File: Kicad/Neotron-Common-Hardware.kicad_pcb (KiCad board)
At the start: 4 copper layers, 243.8 x 243.8 mm, 210 parts, among them J1001 SD_Card, J101 Neotron-Expansion-Slot, J102 Neotron-Expansion-Slot, J103 Neotron-Expansion-Slot, J104 Neotron-Expansion-Slot, J201 DE15HD, J301 RJ45 MagJack, J401 CD Audio In, J402 AC'97 Audio Header, J403 Line Out, J501 USB Ports External, J502 USB Ports Internal, J601 Jack-DC, J602 Conn_01x04, J603 Double-mini-DIN-6, J801 Conn_02x05, J802 DB9_Male_MountingHoles, SW601 SW_DIP_x01, SW602 SW_DIP_x01, U101 Neotron-CPU, U201 THS7316, U202 TPD7S019, U301 ENC424J600, U401 TLV320AIC23BPW, U402 STX-4335-5BGP-S1, U501 AP2501, U502 MIC2005A-2YM5, U503 MIC2005A-2YM5, U504 XR22404CG28, U505 MIC2005A-2YM5, U506 MIC2005A-2YM5, U601 5V DC-DC Module, U602 3v3 LDO, U603 MAX1615, U604 MKE04P24M48SF0, U801 ST3232CDR, U901 MCP7940, Y301 25M, Y401 12M, Y501 12M, Y901 32,768 Hz

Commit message: Updated PCB with latest netlist.
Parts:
- added R301: 24k 0.5%, Resistor_SMD:R_0805_2012Metric_Pad1.15x1.40mm_HandSolder, F.Cu at (54.7, 116.4)
- added R302: 24k 0.5%, Resistor_SMD:R_0805_2012Metric_Pad1.15x1.40mm_HandSolder, F.Cu at (68.9, 116.4)
- added R303: 24k 0.5%, Resistor_SMD:R_0805_2012Metric_Pad1.15x1.40mm_HandSolder, F.Cu at (64.2, 119.3)
- added R304: 24k 0.5%, Resistor_SMD:R_0805_2012Metric_Pad1.15x1.40mm_HandSolder, F.Cu at (59.4, 122.3)
- added R305: 24k 0.5%, Resistor_SMD:R_0805_2012Metric_Pad1.15x1.40mm_HandSolder, F.Cu at (68.9, 113.4)
- added R306: 24k 0.5%, Resistor_SMD:R_0805_2012Metric_Pad1.15x1.40mm_HandSolder, F.Cu at (64.2, 116.4)
- added R307: 12k 0.5%, Resistor_SMD:R_0805_2012Metric_Pad1.15x1.40mm_HandSolder, F.Cu at (59.4, 119.3)
- added R308: 12k 0.5%, Resistor_SMD:R_0805_2012Metric_Pad1.15x1.40mm_HandSolder, F.Cu at (54.7, 122.3)
- added R309: 12k 0.5%, Resistor_SMD:R_0805_2012Metric_Pad1.15x1.40mm_HandSolder, F.Cu at (64.2, 113.4)
- added R310: 12k 0.5%, Resistor_SMD:R_0805_2012Metric_Pad1.15x1.40mm_HandSolder, F.Cu at (59.4, 116.4)
- added R311: 12k 0.5%, Resistor_SMD:R_0805_2012Metric_Pad1.15x1.40mm_HandSolder, F.Cu at (54.7, 113.4)
- added R312: 24k 0.5%, Resistor_SMD:R_0805_2012Metric_Pad1.15x1.40mm_HandSolder, F.Cu at (54.7, 119.3)
- added R313: 3300, Resistor_SMD:R_0805_2012Metric_Pad1.15x1.40mm_HandSolder, F.Cu at (59.4, 113.4)
- added R401: 24k 0.5%, Resistor_SMD:R_0805_2012Metric_Pad1.15x1.40mm_HandSolder, F.Cu at (64.2, 134.6)
- added R402: 24k 0.5%, Resistor_SMD:R_0805_2012Metric_Pad1.15x1.40mm_HandSolder, F.Cu at (59.4, 137.5)
- added R403: 24k 0.5%, Resistor_SMD:R_0805_2012Metric_Pad1.15x1.40mm_HandSolder, F.Cu at (68.9, 128.7)
- added R404: 24k 0.5%, Resistor_SMD:R_0805_2012Metric_Pad1.15x1.40mm_HandSolder, F.Cu at (64.2, 131.6)
- added R405: 24k 0.5%, Resistor_SMD:R_0805_2012Metric_Pad1.15x1.40mm_HandSolder, F.Cu at (59.4, 134.6)
- added R406: 24k 0.5%, Resistor_SMD:R_0805_2012Metric_Pad1.15x1.40mm_HandSolder, F.Cu at (68.9, 131.6)
- added R407: 12k 0.5%, Resistor_SMD:R_0805_2012Metric_Pad1.15x1.40mm_HandSolder, F.Cu at (54.7, 128.7)
- added R408: 12k 0.5%, Resistor_SMD:R_0805_2012Metric_Pad1.15x1.40mm_HandSolder, F.Cu at (54.7, 137.5)
- added R409: 12k 0.5%, Resistor_SMD:R_0805_2012Metric_Pad1.15x1.40mm_HandSolder, F.Cu at (64.2, 128.7)
- added R410: 12k 0.5%, Resistor_SMD:R_0805_2012Metric_Pad1.15x1.40mm_HandSolder, F.Cu at (59.4, 131.6)
- added R411: 12k 0.5%, Resistor_SMD:R_0805_2012Metric_Pad1.15x1.40mm_HandSolder, F.Cu at (54.7, 134.6)
- added R412: 24k 0.5%, Resistor_SMD:R_0805_2012Metric_Pad1.15x1.40mm_HandSolder, F.Cu at (59.4, 128.7)
- added R413: 3300, Resistor_SMD:R_0805_2012Metric_Pad1.15x1.40mm_HandSolder, F.Cu at (54.7, 131.6)
- added R501: 24k 0.5%, Resistor_SMD:R_0805_2012Metric_Pad1.15x1.40mm_HandSolder, F.Cu at (93.7, 116.4)
- added R502: 24k 0.5%, Resistor_SMD:R_0805_2012Metric_Pad1.15x1.40mm_HandSolder, F.Cu at (89.0, 119.3)
- added R503: 24k 0.5%, Resistor_SMD:R_0805_2012Metric_Pad1.15x1.40mm_HandSolder, F.Cu at (84.2, 122.3)
- added R504: 24k 0.5%, Resistor_SMD:R_0805_2012Metric_Pad1.15x1.40mm_HandSolder, F.Cu at (93.7, 113.4)
- added R505: 24k 0.5%, Resistor_SMD:R_0805_2012Metric_Pad1.15x1.40mm_HandSolder, F.Cu at (89.0, 116.4)
- added R506: 24k 0.5%, Resistor_SMD:R_0805_2012Metric_Pad1.15x1.40mm_HandSolder, F.Cu at (84.2, 119.3)
- added R507: 12k 0.5%, Resistor_SMD:R_0805_2012Metric_Pad1.15x1.40mm_HandSolder, F.Cu at (79.5, 122.3)
- added R508: 12k 0.5%, Resistor_SMD:R_0805_2012Metric_Pad1.15x1.40mm_HandSolder, F.Cu at (89.0, 113.4)
- added R509: 12k 0.5%, Resistor_SMD:R_0805_2012Metric_Pad1.15x1.40mm_HandSolder, F.Cu at (84.2, 116.4)
- added R510: 12k 0.5%, Resistor_SMD:R_0805_2012Metric_Pad1.15x1.40mm_HandSolder, F.Cu at (79.5, 119.3)
- added R511: 12k 0.5%, Resistor_SMD:R_0805_2012Metric_Pad1.15x1.40mm_HandSolder, F.Cu at (84.2, 113.4)
- added R512: 24k 0.5%, Resistor_SMD:R_0805_2012Metric_Pad1.15x1.40mm_HandSolder, F.Cu at (79.5, 116.4)
- added R513: 3300, Resistor_SMD:R_0805_2012Metric_Pad1.15x1.40mm_HandSolder, F.Cu at (79.5, 113.4)
- C1006: renamed from C504; footprint Capacitor_THT:CP_Radial_D6.3mm_P2.50mm -> Capacitor_THT:CP_Radial_D8.0mm_P3.50mm
- C1007: renamed from C505; footprint Capacitor_THT:CP_Radial_D6.3mm_P2.50mm -> Capacitor_THT:CP_Radial_D8.0mm_P3.50mm
- C1010: renamed from C509; footprint Capacitor_THT:CP_Radial_D6.3mm_P2.50mm -> Capacitor_THT:CP_Radial_D8.0mm_P3.50mm
- C1011: renamed from C510; footprint Capacitor_THT:CP_Radial_D6.3mm_P2.50mm -> Capacitor_THT:CP_Radial_D8.0mm_P3.50mm
- C901: renamed from C601; footprint Capacitor_THT:CP_Radial_D6.3mm_P2.50mm -> Capacitor_THT:CP_Radial_D8.0mm_P3.50mm
- C902: renamed from C602; footprint Capacitor_THT:CP_Radial_D6.3mm_P2.50mm -> Capacitor_THT:CP_Radial_D8.0mm_P3.50mm
- J802: footprint Connector_Dsub:DSUB-9_Male_Horizontal_P2.77x2.84mm_EdgePinOffset4.94mm_Housed_MountingHolesOffset7.48mm -> Connector_Dsub:DSUB-9_Male_Horizontal_P2.77x2.84mm_EdgePinOffset7.70mm_Housed_MountingHolesOffset9.12mm
- renumbered BT901 to BT1201, C501 to C1001, C508 to C1002, C511 to C1003, C502 to C1004, C503 to C1005, C506 to C1008, C507 to C1009, C310 to C1101, C311 to C1102, C309 to C1103, C312 to C1104, C308 to C1105, C301 to C1106, C302 to C1107, C303 to C1108, C304 to C1109, C305 to C1110, C306 to C1111, C307 to C1112, C901 to C1201, C902 to C1202, C903 to C1203, C412 to C601, C413 to C602, C407 to C603, C411 to C604, C418 to C605, C419 to C606, C424 to C607, C427 to C608, C431 to C609, C435 to C610, C402 to C611, C406 to C612, C408 to C613, C420 to C614, C421 to C615, C426 to C616, C428 to C617, C432 to C618, C437 to C619, C422 to C620, C423 to C621, C430 to C622, C433 to C623, C436 to C624, C438 to C625, C415 to C626, C416 to C627, C401 to C628, C405 to C629, C425 to C630, C429 to C631, C434 to C632, C403 to C633, C409 to C634, C414 to C635, C417 to C636, C404 to C637, C410 to C638, C1001 to C701, C1002 to C702, C802 to C801, C803 to C802, C805 to C803, C801 to C805, C603 to C903, C604 to C904, C605 to C905, C606 to C906, C607 to C907, C608 to C908, D601 to D901, F601 to F901, FB405 to FB601, FB409 to FB602, FB406 to FB603, FB410 to FB604, FB408 to FB605, FB411 to FB606, FB407 to FB607, FB401 to FB608, FB403 to FB609, FB402 to FB610, FB404 to FB611, J501 to J1001, J502 to J1002, J301 to J1101, J403 to J601, J402 to J602, J401 to J603, J1001 to J701, J601 to J901, J602 to J902, J603 to J903, L601 to L901, LOGO103 to LOGO101, LOGO101 to LOGO103, R502 to R1001, R501 to R1002, R503 to R1003, R504 to R1004, R507 to R1005, R508 to R1006, R509 to R1007, R506 to R1008, R302 to R1101, R308 to R1102, R303 to R1103, R304 to R1104, R301 to R1105, R309 to R1106, R305 to R1107, R311 to R1108, R310 to R1109, R312 to R1110, R307 to R1111, R306 to R1112, R209 to R207, R207 to R208, R208 to R209, R404 to R601, R405 to R602, R406 to R603, R409 to R604, R407 to R605, R410 to R606, R414 to R607, R415 to R608, R408 to R609, R413 to R610, R411 to R611, R412 to R612, R416 to R613, R401 to R614, R403 to R615, R402 to R616, R601 to R901, R602 to R902, R603 to R903, R604 to R904, R606 to R905, R605 to R906, R608 to R907, R607 to R908, RN1001 to RN701, RN601 to RN901, SW601 to SW901, SW602 to SW902, TP601 to TP901, U501 to U1001, U502 to U1002, U503 to U1003, U504 to U1004, U505 to U1005, U506 to U1006, U301 to U1101, U901 to U1201, U401 to U601, U402 to U602, U601 to U901, U602 to U902, U603 to U903, U604 to U904, Y501 to Y1001, Y301 to Y1101, Y901 to Y1201, Y401 to Y601

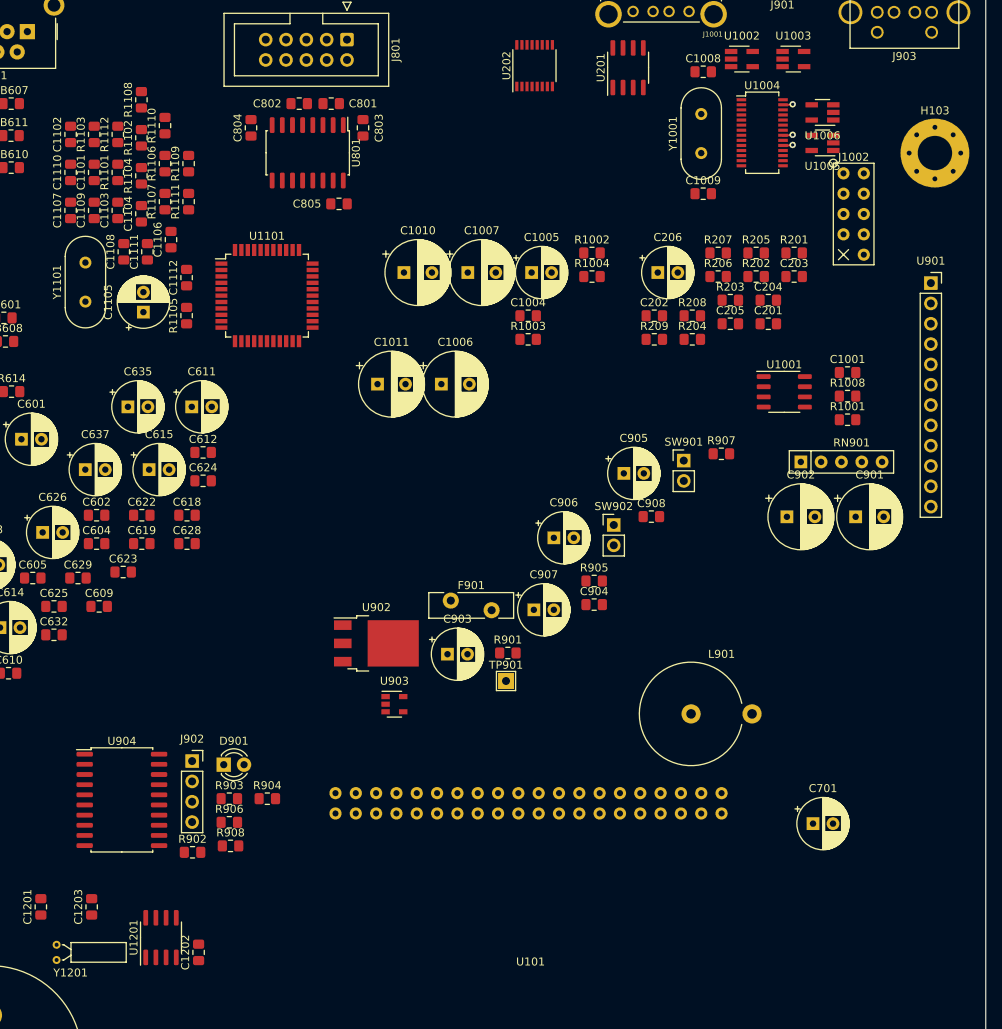
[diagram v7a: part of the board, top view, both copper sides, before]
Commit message: Tweaking some 3D models.
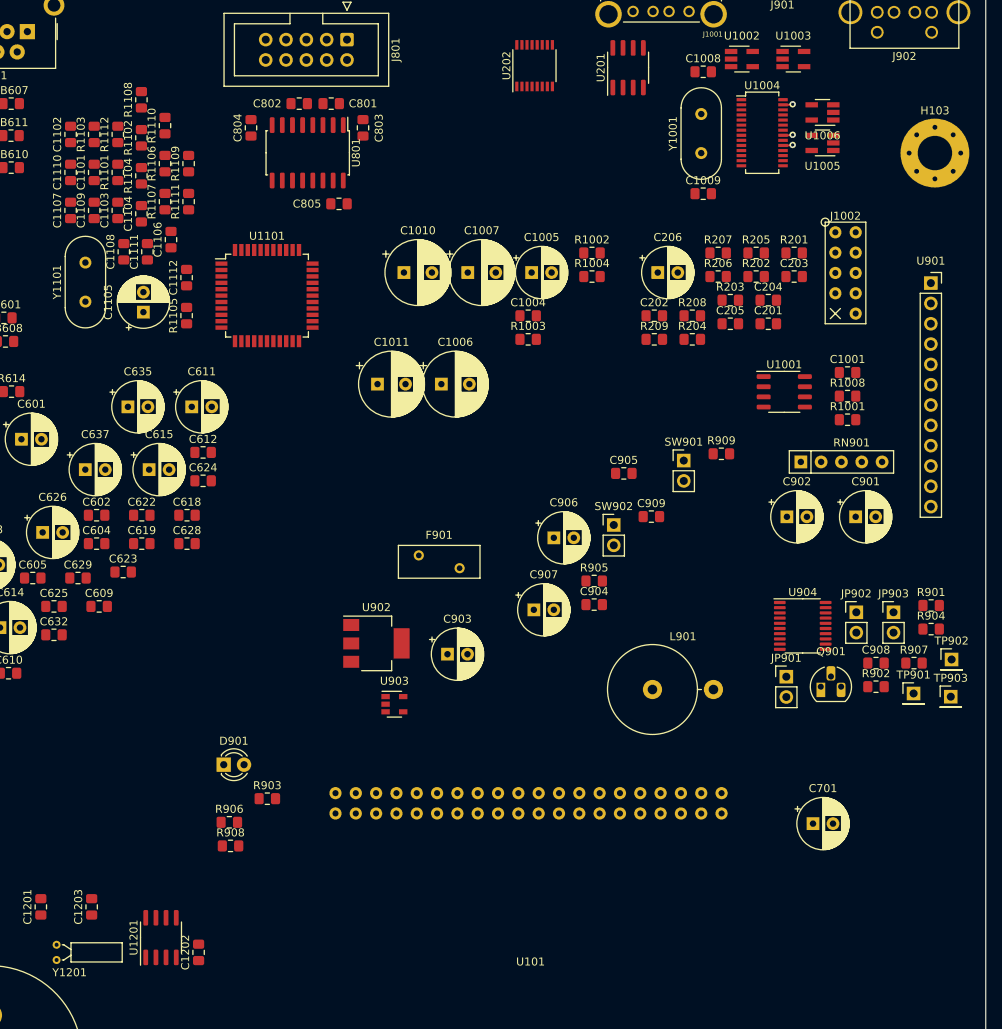
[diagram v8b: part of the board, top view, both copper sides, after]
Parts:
- removed the J902 at (178.4, 140.2)
- removed the R903 at (183.1, 144.9)
- added C908: 100n, Capacitor_SMD:C_0805_2012Metric_Pad1.15x1.40mm_HandSolder, F.Cu at (263.9, 128.0)
- added JP901: Jumper, Connector_PinHeader_2.54mm:PinHeader_1x02_P2.54mm_Vertical, F.Cu at (252.7, 129.7)
- added JP902: Jumper, Connector_PinHeader_2.54mm:PinHeader_1x02_P2.54mm_Vertical, F.Cu at (261.4, 121.6)
- added JP903: Jumper, Connector_PinHeader_2.54mm:PinHeader_1x02_P2.54mm_Vertical, F.Cu at (266.1, 121.6)
- added Q901: BC548, Package_TO_SOT_THT:TO-92_HandSolder, F.Cu at (257.0, 130.9)
- added R904: 10k, Resistor_SMD:R_0805_2012Metric_Pad1.15x1.40mm_HandSolder, F.Cu at (270.8, 123.7)
- added R907: 10k, Resistor_SMD:R_0805_2012Metric_Pad1.15x1.40mm_HandSolder, F.Cu at (268.6, 128.0)
- added TP902: TestPoint, Connector_PinHeader_2.54mm:PinHeader_1x01_P2.54mm_Vertical, F.Cu at (273.3, 127.5)
- added TP903: TestPoint, Connector_PinHeader_2.54mm:PinHeader_1x01_P2.54mm_Vertical, F.Cu at (273.2, 132.2)
- C901, C902: footprint Capacitor_THT:CP_Radial_D8.0mm_P3.50mm -> Capacitor_THT:CP_Radial_D6.3mm_P2.50mm
- C905: value 47u -> 1u; footprint Capacitor_THT:CP_Radial_D6.3mm_P2.50mm -> Capacitor_SMD:C_0805_2012Metric_Pad1.15x1.40mm_HandSolder
- F901: value 6A PTC -> 32V 2A PTC; footprint Fuse:Fuse_Bourns_MF-RG500 -> Fuse:Fuse_BelFuse_0ZRE0016FF_L9.9mm_W3.8mm
- L901: value 22u -> 22uH 6A; footprint Inductor_THT:L_Axial_L23.4mm_D12.7mm_P7.62mm_Vertical_Vishay_IHA-203 -> Inductor_THT:L_Axial_L26.0mm_D11.0mm_P7.62mm_Vertical_Fastron_77A
- R901: value 100k -> 2k
- R902, R905, R908: value 100k -> 10k
- R906: value 33k -> 10k
- R909: renamed from R907; value 100k -> 10k
- TP901: value Reset -> TestPoint; footprint TestPoint:TestPoint_THTPad_2.0x2.0mm_Drill1.0mm -> Connector_PinHeader_2.54mm:PinHeader_1x01_P2.54mm_Vertical
- U902: value 3v3 LDO -> TLV1117 3.3V 1A; footprint Package_TO_SOT_SMD:TO-252-3_TabPin2 -> Package_TO_SOT_SMD:SOT-223-3_TabPin2
- U904: value MKE04P24M48SF0 -> STM32F030F4Px; footprint Package_SO:SOIC-20W_7.5x12.8mm_P1.27mm -> Package_SO:TSSOP-20_4.4x6.5mm_P0.65mm
- Y1201: footprint Crystal:Crystal_C26-LF_D2.1mm_L6.5mm_Horizontal -> Crystal:Crystal_DS26_D2.0mm_L6.0mm_Horizontal
- moved R902 87.9 mm to (263.9, 130.9)
- moved U904 87.8 mm to (254.7, 123.3)
- moved R901 53.2 mm to (270.8, 120.8)
- moved TP901 51.0 mm to (268.6, 131.8)
- moved J1002 7.44 mm to (260.1, 71.6)
- moved F901 6.92 mm to (206.7, 114.5)
- moved L901 5.71 mm to (235.9, 131.3)
- renumbered C908 to C909, J903 to J902, R904 to R903
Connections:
- C907 pad 1: +5VP -> +3.3VP
- C909 pad 1: +5VP -> +3.3VP
- R901 pad 1: /Power Supply/DC_ON -> Net-(Q901-Pad2)
- R901 pad 2: GND -> /Power Supply/DC_ON
- R902 pad 1: +5VP -> /Power Supply/DC_ON
- R902 pad 2: /Power Supply/SWDCLK -> GND
- R903 pad 1: /Power Supply/STATUS_LED -> /Power Supply/~STATUS_LED
- R905 pad 2: /Power Supply/MON_5V -> Net-(R905-Pad2)
- SW901 pad 2: /Power Supply/~RESET_SW -> /Power Supply/~BUTTON_RST
- SW902 pad 2: /Power Supply/~POWER_SW -> /Power Supply/~BUTTON_PWR
- TP901 pad 1: Net-(TP901-Pad1) -> /Power Supply/USART1_TX
- U901 pad 1: /Power Supply/DC_ON -> /Power Supply/~PSU_EN
- U903 pad 3: +5VP -> +3.3VP
- U903 pad 4: +5VP -> GND
- U904 pad 1: Net-(TP901-Pad1) -> /Power Supply/BOOT0
- U904 pad 10: /Power Supply/PS2_CLK1 -> /Power Supply/DC_ON
- U904 pad 11: /Power Supply/PS2_DAT0 -> (no net)
- U904 pad 12: /Power Supply/PS2_CLK0 -> /Power Supply/~BUTTON_RST
- U904 pad 13: /Power Supply/~RESET_SW -> /Power Supply/~BUTTON_PWR
- U904 pad 15: /Power Supply/UART0_TX -> GND
- U904 pad 16: /Power Supply/MON_3V3 -> +3.3VP
- U904 pad 17: (no net) -> /Power Supply/SCL_U1TX
- U904 pad 18: (no net) -> /Power Supply/SDA_U1RX
- U904 pad 19: /Power Supply/MON_5V -> /Power Supply/PS2_DAT1
- U904 pad 2: /Power Supply/SWDIO -> /Power Supply/PS2_DAT0
- U904 pad 20: /Power Supply/SWDCLK -> /Power Supply/PS2_CLK1
- U904 pad 3: +5VP -> /Power Supply/PS2_CLK0
- U904 pad 4: GND -> /Power Supply/~BMC_RST
- U904 pad 5: /Power Supply/STATUS_LED -> +3.3VP
- U904 pad 6: /Power Supply/DC_ON -> /Power Supply/MON_3V3
- U904 pad 7: (no net) -> /Power Supply/MON_5V
- U904 pad 8: /Power Supply/~POWER_SW -> /Power Supply/USART1_TX
- U904 pad 9: /Power Supply/PS2_DAT1 -> /Power Supply/~STATUS_LED
